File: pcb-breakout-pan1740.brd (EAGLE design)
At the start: 30.5 x 23 mm, 3 parts, among them IC1 PAN1740

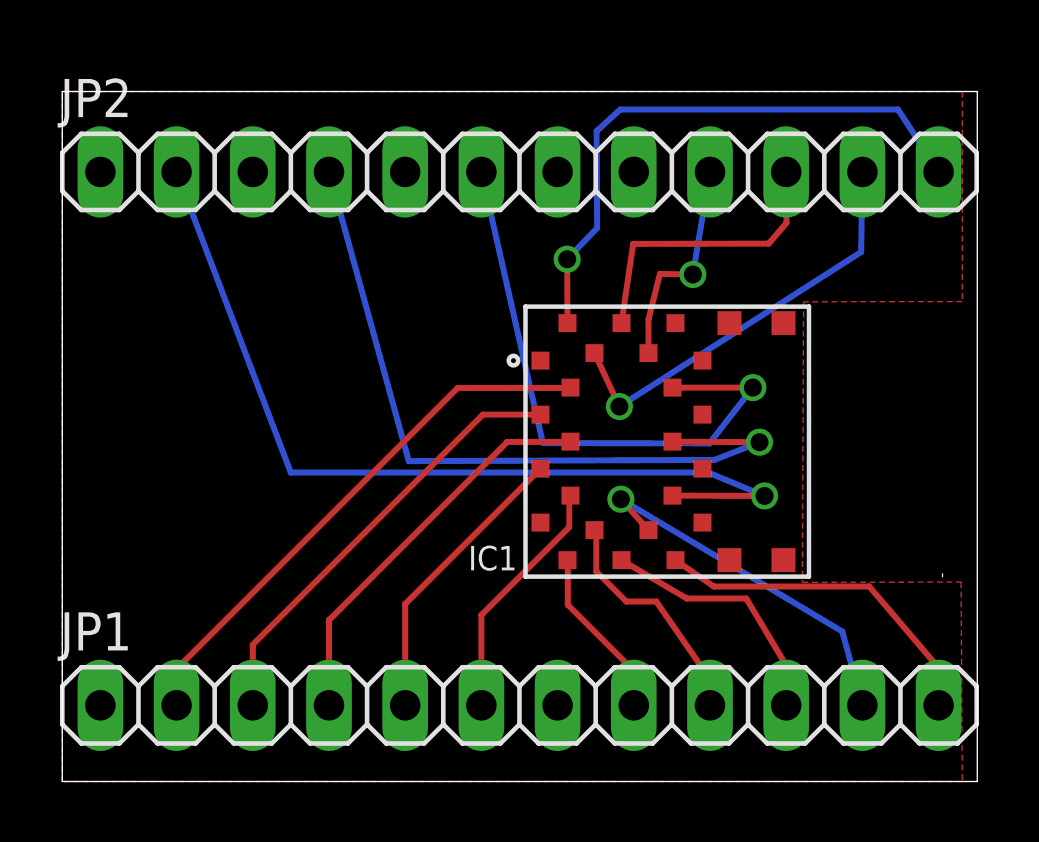
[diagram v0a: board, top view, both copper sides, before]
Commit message: polygon adjustment
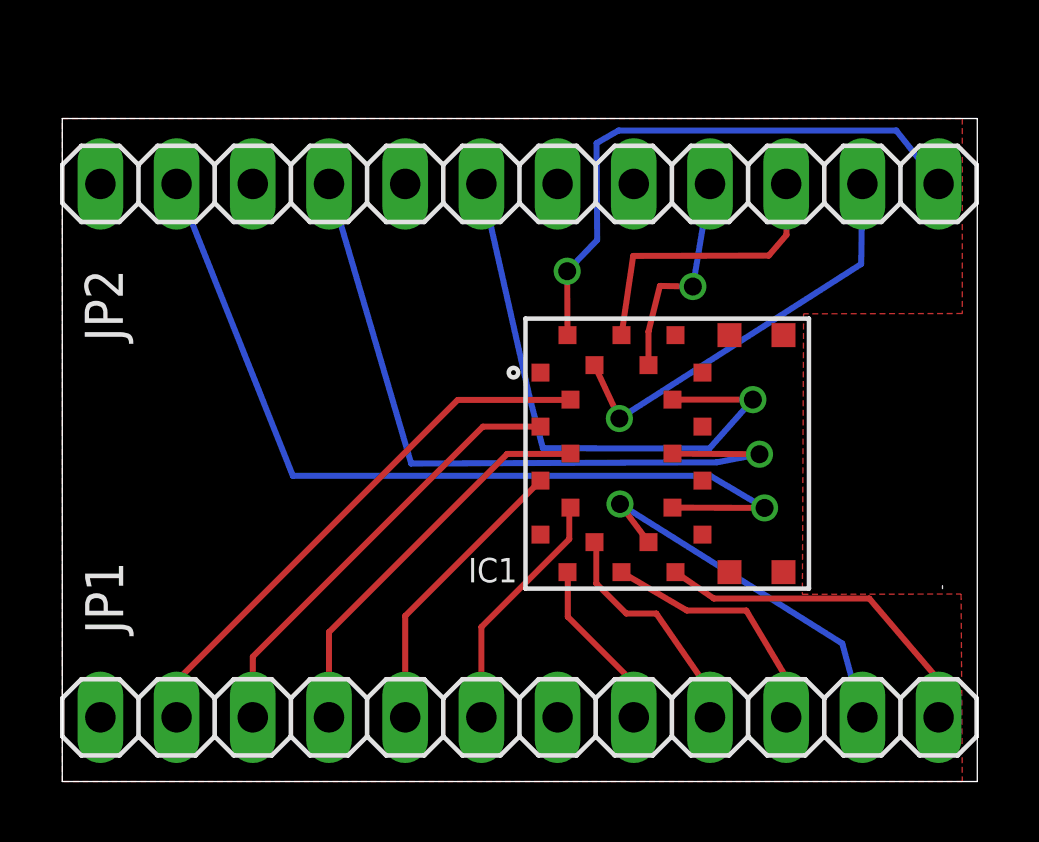
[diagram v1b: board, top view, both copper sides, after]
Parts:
- moved IC1 0.40 mm to (20.1, 10.9)
- moved JP1 0.40 mm to (15.2, 2.14)
- moved JP2 0.40 mm to (15.2, 19.9)
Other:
- board size 30.5 x 23 mm -> 30.5 x 22.1 mm

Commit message: silkscreen
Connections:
- net GND: now also JP1.7, JP2.3, JP2.5, JP2.7, JP2.8
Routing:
- net N$15: track 7.25 -> 6.63 mm
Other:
- board text added: "GND"
- board text added: "P0.0"
- board text added: "P0.1"
- board text added: "P0.2"
- board text added: "P0.3"
- board text added: "P0.4"
- board text added: "P0.5"
- board text added: "P0.6"
- board text added: "P0.7"
- board text added: "P1.0"
- board text added: "P1.1"
- board text added: "P1.2"
- board text added: "P1.3"
- board text added: "RST"
- board text added: "SWCLK/P1_4"
- board text added: "SW_DIO/P1_5"
- board text added: "VCC"
- board text added: "VPP"
- board text added: "n.c"
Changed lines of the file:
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@@
 <drawing>
 <settings>
-<setting alwaysvectorfont="no"/>
+<setting alwaysvectorfont="yes"/>
 <setting verticaltext="up"/>
 </settings>
-<grid distance="1" unitdist="mm" unit="mm" style="lines" multiple="1" display="no" altdistance="0.01" altunitdist="mm" altunit="mm"/>
+<grid distance="2.54" unitdist="mm" unit="mm" style="lines" multiple="1" display="no" altdistance="0.01" altunitdist="mm" altunit="mm"/>
 <layers>
 <layer number="1" name="Top" color="4" fill="1" visible="yes" active="yes"/>
@@
 <wire x1="30.5" y1="22.1" x2="0" y2="22.1" width="0" layer="20"/>
 <wire x1="0" y1="22.1" x2="0" y2="0" width="0" layer="20"/>
+<text x="1.65" y="3.82" size="0.8128" layer="21" rot="R90">GND</text>
+<text x="4.19" y="3.82" size="0.8128" layer="21" rot="R90">RST</text>
+<text x="6.73" y="3.82" size="0.8128" layer="21" rot="R90">P0.7</text>
+<text x="9.27" y="3.82" size="0.8128" layer="21" rot="R90">P0.6</text>
+<text x="11.81" y="3.82" size="0.8128" layer="21" rot="R90">P0.5</text>
+<text x="14.35" y="3.82" size="0.8128" layer="21" rot="R90">P0.4</text>
+<text x="16.89" y="3.82" size="0.8128" layer="21" rot="R90">GND</text>
+<text x="19.43" y="3.82" size="0.8128" layer="21" rot="R90">VCC</text>
+<text x="21.97" y="3.82" size="0.8128" layer="21" rot="R90">P0.3</text>
+<text x="24.51" y="3.82" size="0.8128" layer="21" rot="R90">P0.2</text>
+<text x="27.05" y="3.82" size="0.8128" layer="21" rot="R90">P0.1</text>
+<text x="29.59" y="3.82" size="0.8128" layer="21" rot="R90">P0.0</text>
+<text x="0.87" y="18.38" size="0.8128" layer="21" rot="R270">n.c</text>
+<text x="3.41" y="18.38" size="0.8128" layer="21" rot="R270">VPP</text>
+<text x="5.95" y="18.38" size="0.8128" layer="21" rot="R270">GND</text>
+<text x="8.49" y="18.38" size="0.8128" layer="21" rot="R270">SWCLK/P1_4</text>
+<text x="11.03" y="18.38" size="0.8128" layer="21" rot="R270">GND</text>
+<text x="13.57" y="18.38" size="0.8128" layer="21" rot="R270">SW_DIO/P1_5</text>
+<text x="21.19" y="18.38" size="0.8128" layer="21" rot="R270">P1.3</text>
+<text x="17.54" y="18.38" size="0.8128" layer="21" rot="R270">GND</text>
+<text x="23.73" y="18.38" size="0.8128" layer="21" rot="R270">P1.2</text>
+<text x="26.27" y="18.38" size="0.8128" layer="21" rot="R270">P1.1</text>
+<text x="28.81" y="18.38" size="0.8128" layer="21" rot="R270">P1.0</text>
 </plain>
 <attributes>
@@
 <elements>
 <element name="IC1" library="panasonic-pan1740" package="PAN1740" value="PAN1740" x="20.14" y="10.93" smashed="yes">
-<attribute name="NAME" x="13.53" y="6.64" size="0.8128" layer="25" font="vector"/>
-<attribute name="VALUE" x="14.44" y="13.31" size="0.8128" layer="27" font="vector" rot="R270"/>
+<attribute name="NAME" x="15.12" y="7.26" size="0.8128" layer="25" font="vector" rot="R90"/>
+<attribute name="VALUE" x="30.34" y="8.68" size="0.8128" layer="27" font="vector" rot="R90"/>
 </element>
 <element name="JP1" library="pinhead" package="1X12" value="" x="15.24" y="2.14" smashed="yes">
-<attribute name="NAME" x="2.0312" y="4.9238" size="1.27" layer="25" ratio="10" rot="R90"/>
+<attribute name="NAME" x="10.21" y="6.72" size="1.016" layer="25" ratio="10"/>
 <attribute name="VALUE" x="0" y="-1.035" size="1.27" layer="27"/>
 </element>
 <element name="JP2" library="pinhead" package="1X12" value="" x="15.24" y="19.92" smashed="yes">
-<attribute name="NAME" x="0.7488" y="17.0762" size="1.27" layer="25" ratio="10" rot="R270"/>
+<attribute name="NAME" x="10.1" y="14.6" size="1.016" layer="25" ratio="10"/>
 <attribute name="VALUE" x="0" y="16.745" size="1.27" layer="27"/>
 </element>
@@
 <contactref element="IC1" pad="21"/>
 <contactref element="JP2" pad="9"/>
-<wire x1="21.59" y1="19.92" x2="21.02" y2="16.5" width="0.2" layer="16"/>
-<via x="21.02" y="16.5" extent="1-16" drill="0.6" shape="square"/>
-<wire x1="21.02" y1="16.5" x2="19.92" y2="16.52" width="0.2" layer="1"/>
-<wire x1="19.92" y1="16.52" x2="19.54" y2="15" width="0.2" layer="1"/>
-<wire x1="19.54" y1="15" x2="19.54" y2="13.88" width="0.2" layer="1"/>
+<wire x1="21.59" y1="19.92" x2="19.55" y2="16.72" width="0.2" layer="16"/>
+<wire x1="19.55" y1="16.72" x2="19.54" y2="13.88" width="0.2" layer="1"/>
+<via x="19.55" y="16.72" extent="1-16" drill="0.6" shape="square"/>
 </signal>
 <signal name="N$16">
@@
 <contactref element="JP2" pad="10"/>
 <wire x1="24.13" y1="19.92" x2="24.14" y2="18.22" width="0.2" layer="1"/>
-<wire x1="24.14" y1="18.22" x2="23.55" y2="17.53" width="0.2" layer="1"/>
-<wire x1="23.55" y1="17.53" x2="19.03" y2="17.52" width="0.2" layer="1"/>
-<wire x1="19.03" y1="17.52" x2="18.64" y2="14.88" width="0.2" layer="1"/>
+<wire x1="24.14" y1="18.22" x2="23.62" y2="17.61" width="0.2" layer="1"/>
+<wire x1="23.62" y1="17.61" x2="18.65" y2="17.63" width="0.2" layer="1"/>
+<wire x1="18.65" y1="17.63" x2="18.64" y2="14.88" width="0.2" layer="1"/>
 </signal>
 <signal name="N$17">
@@
 <vertex x="0" y="0"/>
 </polygon>
+<contactref element="JP1" pad="7"/>
+<contactref element="JP2" pad="3"/>
+<contactref element="JP2" pad="5"/>
+<contactref element="JP2" pad="7"/>
+<contactref element="JP2" pad="8"/>
 </signal>
 </signals>
